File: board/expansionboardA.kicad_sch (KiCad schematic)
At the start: 66 parts, among them J1 DEBUG, J2 USB_A_Stacked, J3 HDMI_A, J4 FAN, J5 Conn_02x06_Odd_Even, J6 Conn_02x06_Odd_Even, J7 DEBUG, P1 USB_C_Plug, U1 MAX3420EECJ, U2 GPIO_U2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

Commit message: Updated board files
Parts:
- removed J5: Conn_02x06_Odd_Even, Connector_PinSocket_2.54mm:PinSocket_2x06_P2.54mm_Vertical, symbol Connector_Generic:Conn_02x06_Odd_Even
- removed J7: DEBUG, Connector_PinSocket_2.54mm:PinSocket_1x04_P2.54mm_Vertical, symbol Connector_Generic:Conn_01x04
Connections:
- net EX1 is gone; now on net LED1: U4.58 (Pin_58)
- net EX3 is gone; now on net LED2: U4.56 (Pin_56)
- net EX5 is gone; now on net LED3: U4.54 (Pin_54)
- net LED0: now also U4.60 (Pin_60); no longer U2.43 (Pin_43)
- net LED1: no longer U2.45 (Pin_45)
- net LED2: no longer U2.47 (Pin_47)
- net LED3: no longer U2.49 (Pin_49)
- net EX0: no longer names the net of U4.57 (Pin_57)
- net EX2: no longer names the net of U4.55 (Pin_55)
- net EX4: no longer names the net of U4.53 (Pin_53)
- net EX6: no longer names the net of U4.51 (Pin_51)
- net EX7: no longer names the net of U4.52 (Pin_52)
- net EX8: no longer names the net of U4.49 (Pin_49)
- net EX9: no longer names the net of U4.50 (Pin_50)
- net RXD2: no longer names the net of U4.24 (Pin_24)
- net TXD2: no longer names the net of U4.26 (Pin_26)
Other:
- note removed: "Expansion Port A"
- note removed: "UART Port B"

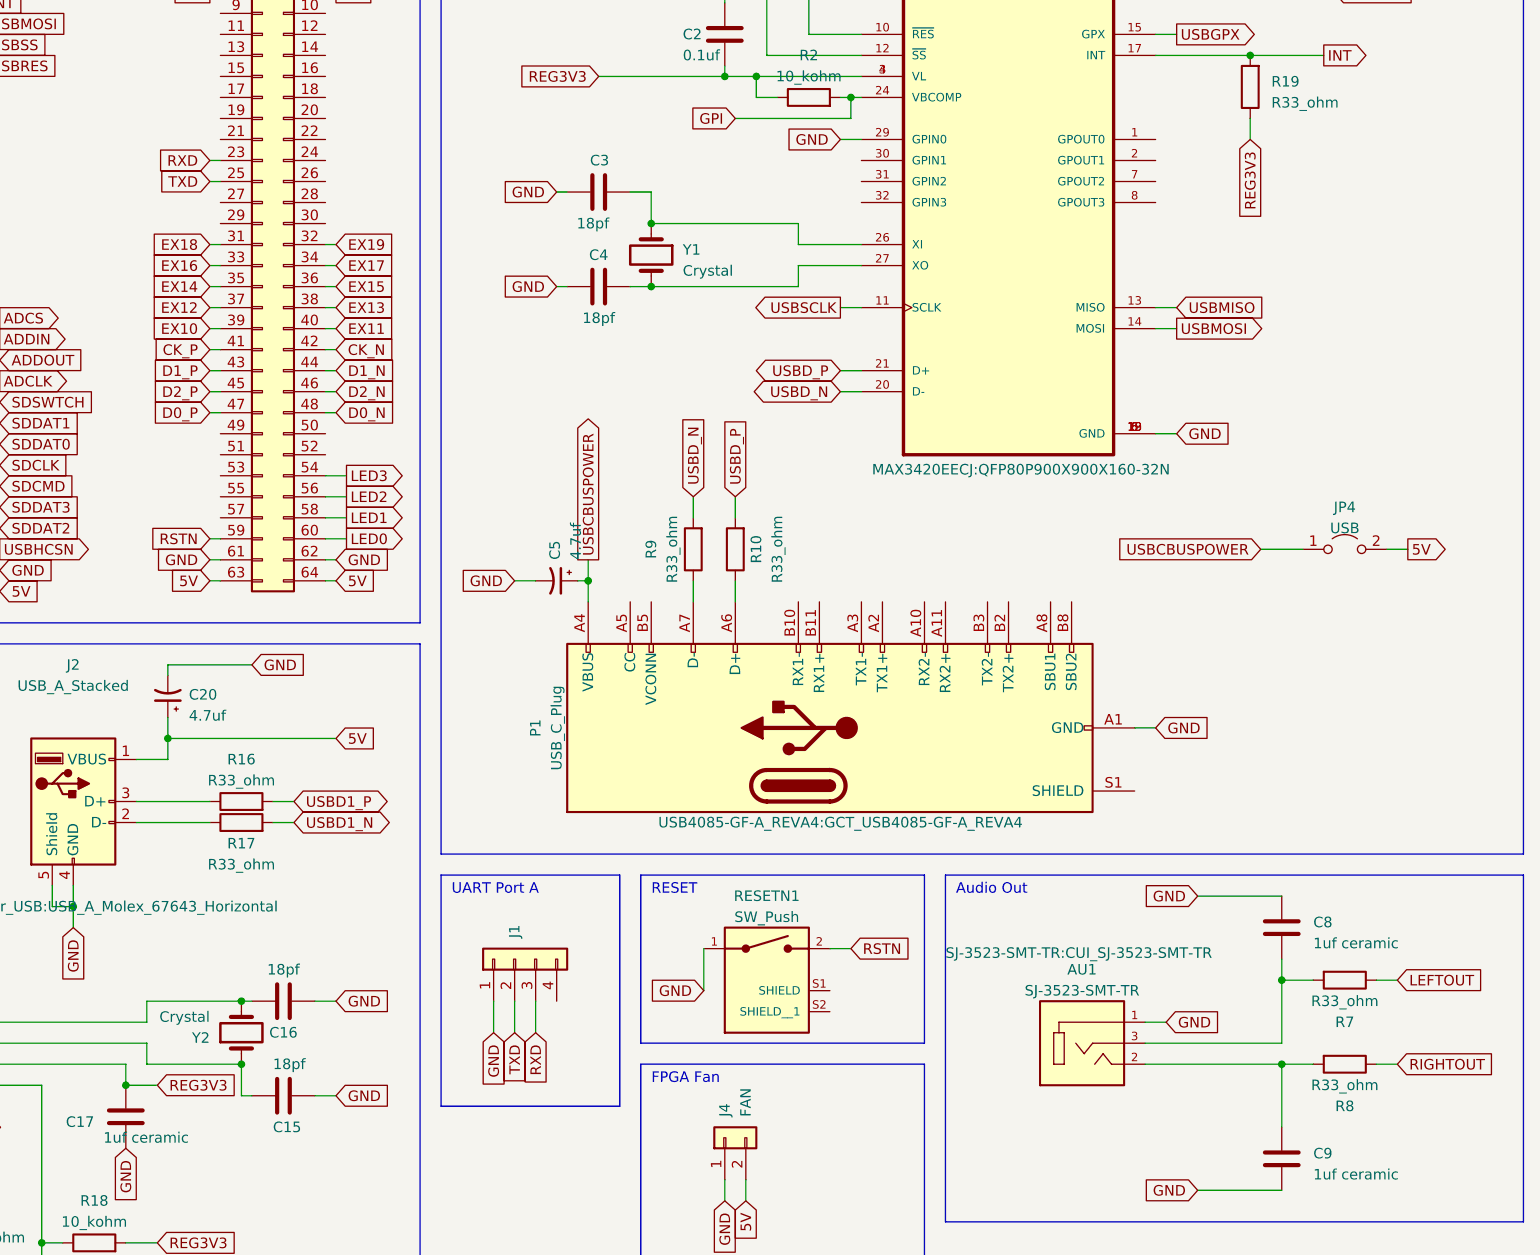
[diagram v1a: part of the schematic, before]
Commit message: Removed UART port from board and SoC
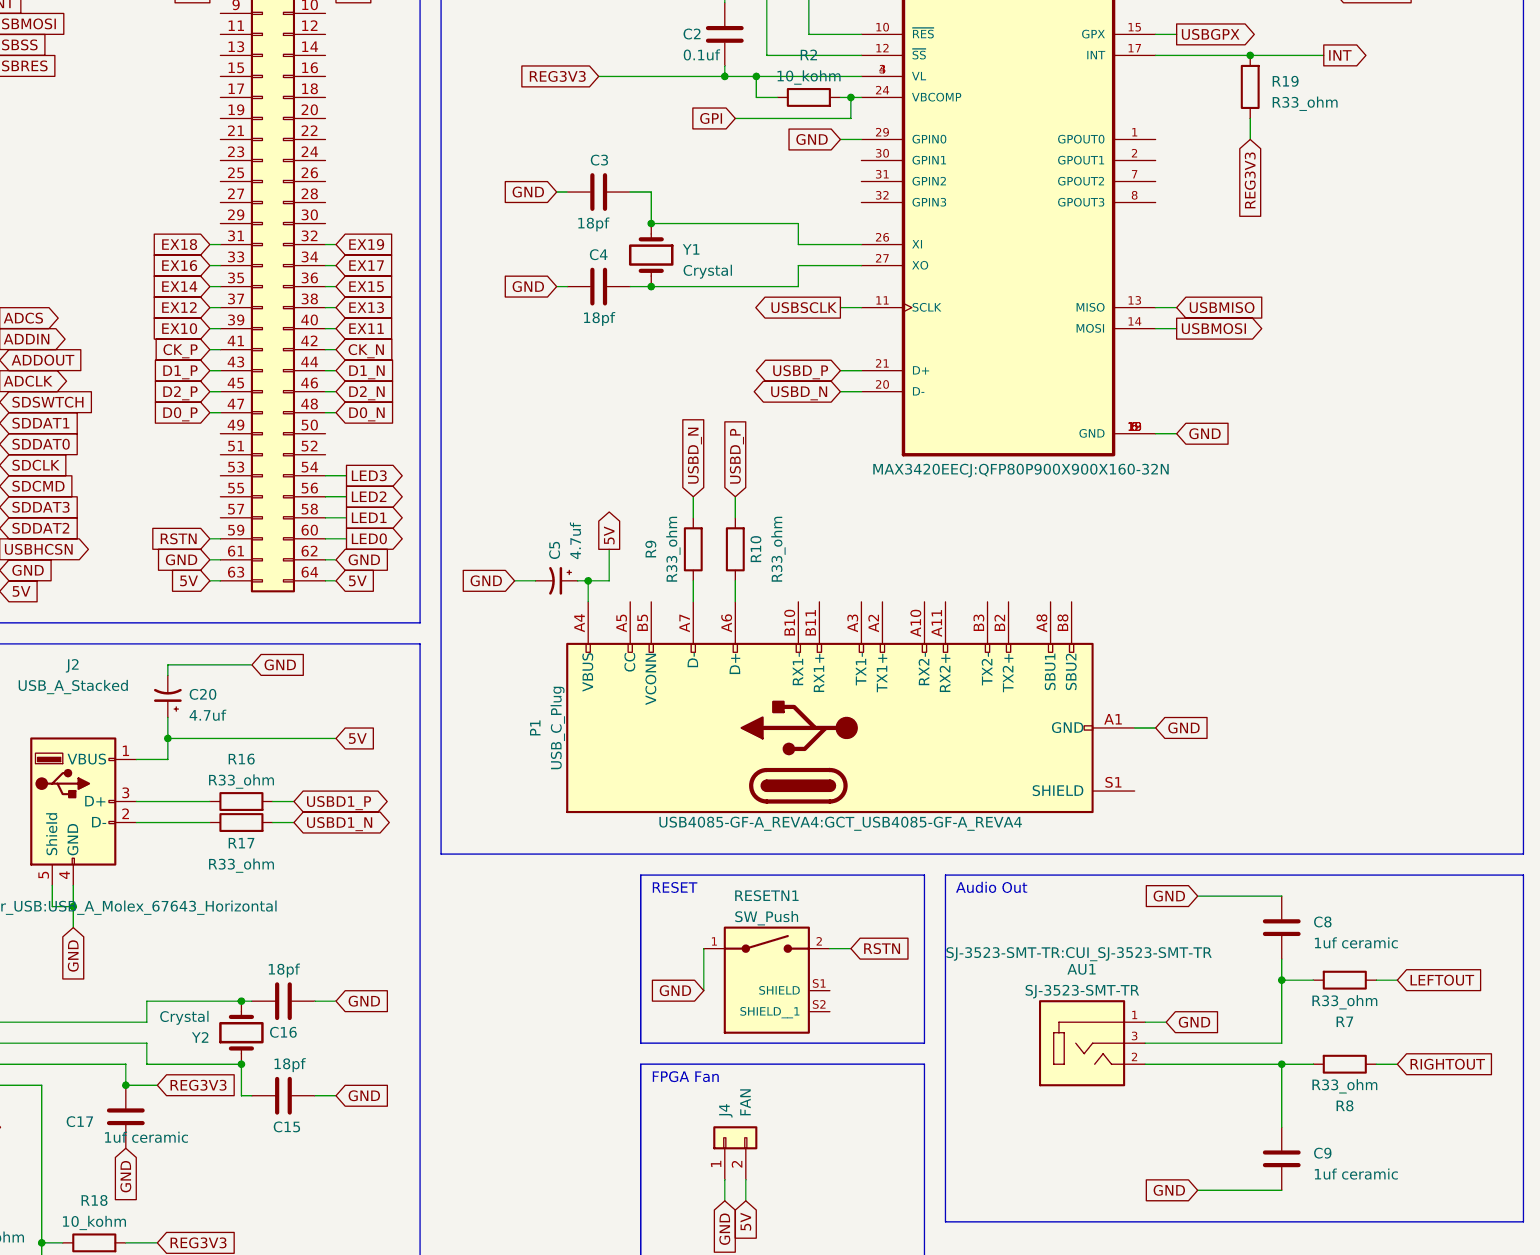
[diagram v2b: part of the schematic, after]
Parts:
- removed J1: DEBUG, Connector_PinSocket_2.54mm:PinSocket_1x04_P2.54mm_Horizontal, symbol Connector_Generic:Conn_01x04
- removed JP4: USB, Jumper:SolderJumper-2_P1.3mm_Open_Pad1.0x1.5mm, symbol Jumper:Jumper_2_Open
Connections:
- net USBCBUSPOWER is gone; now on net 5V: C5.1, P1.A4 (VBUS), P1.A9 (VBUS), P1.B4 (VBUS), P1.B9 (VBUS)
- net RXD: no longer names the net of U4.23 (Pin_23)
- net TXD: no longer names the net of U4.25 (Pin_25)
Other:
- note removed: "UART Port A"
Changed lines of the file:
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@@
     (stroke (width 0) (type default))
   )
-  (wire (pts (xy 387.35 152.4) (xy 389.89 152.4))
-    (stroke (width 0) (type default))
-  )
   (wire (pts (xy 215.9 147.32) (xy 219.71 147.32))
     (stroke (width 0) (type default))
@@
     (stroke (width 0) (type default))
   )
-  (wire (pts (xy 281.94 210.82) (xy 281.94 207.01))
-    (stroke (width 0) (type default))
-  )
   (wire (pts (xy 369.57 57.15) (xy 370.84 57.15))
     (stroke (width 0) (type default))
@@
     (stroke (width 0) (type default))
   )
-  (wire (pts (xy 284.48 210.82) (xy 284.48 207.01))
-    (stroke (width 0) (type default))
-  )
   (wire (pts (xy 219.71 129.54) (xy 215.9 129.54))
     (stroke (width 0) (type default))
   )
-  (wire (pts (xy 290.83 156.21) (xy 290.83 153.67))
+  (wire (pts (xy 293.37 156.21) (xy 293.37 152.4))
     (stroke (width 0) (type default))
   )
@@
     (stroke (width 0) (type default))
   )
-  (wire (pts (xy 372.11 152.4) (xy 377.19 152.4))
-    (stroke (width 0) (type default))
-  )
   (wire (pts (xy 359.41 173.99) (xy 356.87 173.99))
     (stroke (width 0) (type default))
@@
     (stroke (width 0) (type default))
   )
-  (wire (pts (xy 245.11 107.95) (xy 246.38 107.95))
-    (stroke (width 0) (type default))
-  )
   (wire (pts (xy 165.1 35.56) (xy 170.18 35.56))
     (stroke (width 0) (type default))
@@
     (stroke (width 0) (type default))
   )
-  (wire (pts (xy 245.11 105.41) (xy 246.38 105.41))
-    (stroke (width 0) (type default))
-  )
-  (wire (pts (xy 279.4 210.82) (xy 279.4 207.01))
-    (stroke (width 0) (type default))
-  )
   (wire (pts (xy 245.11 151.13) (xy 246.38 151.13))
     (stroke (width 0) (type default))
@@
     (stroke (width 0) (type default))
   )
+  (wire (pts (xy 293.37 156.21) (xy 290.83 156.21))
+    (stroke (width 0) (type default))
+  )
   (wire (pts (xy 378.46 49.53) (xy 381 49.53))
     (stroke (width 0) (type default))
@@
     (fill (type none))
   )
-  (rectangle (start 273.05 191.77) (end 294.64 219.71)
-    (stroke (width 0) (type default))
-    (fill (type none))
-  )
   (rectangle (start 129.54 163.83) (end 270.51 252.73)
     (stroke (width 0) (type default))
@@
     (fill (type none))
   )
-  (text "UART Port A" (at 274.32 194.31 0)
-    (effects (font (size 1.27 1.27)) (justify left bottom))
-  )
   (text "Audio Output" (at 298.45 17.78 0)
     (effects (font (size 1.27 1.27)) (justify left bottom))
@@
     )
   )
-  (global_label "USBCBUSPOWER" (shape input) (at 372.11 152.4 180) (fields_autoplaced)
-    (effects (font (size 1.27 1.27)) (justify right))
-    (property "Intersheetrefs" "${INTERSHEET_REFS}" (at 353.8433 152.4 0)
-      (effects (font (size 1.27 1.27)) (justify right) hide)
-    )
-  )
   (global_label "ADCH4" (shape input) (at 80.01 64.77 180) (fields_autoplaced)
     (effects (font (size 1.27 1.27)) (justify right))
@@
     )
   )
-  (global_label "TXD" (shape input) (at 281.94 210.82 270) (fields_autoplaced)
-    (effects (font (size 1.27 1.27)) (justify right))
-    (property "Intersheetrefs" "${INTERSHEET_REFS}" (at 281.94 217.1729 90)
-      (effects (font (size 1.27 1.27)) (justify right) hide)
-    )
-  )
   (global_label "VCC" (shape input) (at 245.11 80.01 180) (fields_autoplaced)
     (effects (font (size 1.27 1.27)) (justify right))
@@
     )
   )
-  (global_label "RXD" (shape input) (at 245.11 105.41 180) (fields_autoplaced)
-    (effects (font (size 1.27 1.27)) (justify right))
-    (property "Intersheetrefs" "${INTERSHEET_REFS}" (at 238.4547 105.41 0)
-      (effects (font (size 1.27 1.27)) (justify right) hide)
-    )
-  )
   (global_label "GND" (shape input) (at 234.95 224.79 270) (fields_autoplaced)
     (effects (font (size 1.27 1.27)) (justify right))
@@
     )
   )
-  (global_label "GND" (shape input) (at 279.4 210.82 270) (fields_autoplaced)
-    (effects (font (size 1.27 1.27)) (justify right))
-    (property "Intersheetrefs" "${INTERSHEET_REFS}" (at 279.4 217.5963 90)
-      (effects (font (size 1.27 1.27)) (justify right) hide)
-    )
-  )
   (global_label "EX11" (shape input) (at 157.48 104.14 180) (fields_autoplaced)
     (effects (font (size 1.27 1.27)) (justify right))
@@
     )
   )
-  (global_label "USBCBUSPOWER" (shape output) (at 290.83 153.67 90) (fields_autoplaced)
+  (global_label "5V" (shape output) (at 293.37 152.4 90) (fields_autoplaced)
     (effects (font (size 1.27 1.27)) (justify left))
-    (property "Intersheetrefs" "${INTERSHEET_REFS}" (at 290.83 135.4033 90)
+    (property "Intersheetrefs" "${INTERSHEET_REFS}" (at 293.37 147.1961 90)
       (effects (font (size 1.27 1.27)) (justify left) hide)
     )
@@
     )
   )
-  (global_label "TXD" (shape input) (at 245.11 107.95 180) (fields_autoplaced)
-    (effects (font (size 1.27 1.27)) (justify right))
-    (property "Intersheetrefs" "${INTERSHEET_REFS}" (at 238.7571 107.95 0)
-      (effects (font (size 1.27 1.27)) (justify right) hide)
-    )
-  )
   (global_label "AU_SCLK" (shape input) (at 311.15 29.21 180) (fields_autoplaced)
     (effects (font (size 1.27 1.27)) (justify right))
@@
     )
   )
-  (global_label "RXD" (shape input) (at 284.48 210.82 270) (fields_autoplaced)
-    (effects (font (size 1.27 1.27)) (justify right))
-    (property "Intersheetrefs" "${INTERSHEET_REFS}" (at 284.48 217.4753 90)
-      (effects (font (size 1.27 1.27)) (justify right) hide)
-    )
-  )
   (global_label "D1_P" (shape input) (at 96.52 199.39 180) (fields_autoplaced)
     (effects (font (size 1.27 1.27)) (justify right))
@@
     )
   )
-  (global_label "5V" (shape output) (at 389.89 152.4 0) (fields_autoplaced)
-    (effects (font (size 1.27 1.27)) (justify left))
-    (property "Intersheetrefs" "${INTERSHEET_REFS}" (at 395.0939 152.4 0)
-      (effects (font (size 1.27 1.27)) (justify left) hide)
-    )
-  )
   (global_label "USBGPX" (shape output) (at 361.95 90.17 0) (fields_autoplaced)
     (effects (font (size 1.27 1.27)) (justify left))
@@
     )
   )
-  (symbol (lib_id "Connector_Generic:Conn_01x04") (at 281.94 201.93 90) (unit 1)
-    (in_bom yes) (on_board yes) (dnp no)
-    (property "Reference" "J1" (at 281.9399 199.39 0)
-      (effects (font (size 1.27 1.27)) (justify left))
-    )
-    (property "Value" "DEBUG" (at 284.4799 199.39 0)
-      (effects (font (size 1.27 1.27)) (justify left) hide)
-    )
-    (property "Footprint" "Connector_PinSocket_2.54mm:PinSocket_1x04_P2.54mm_Horizontal" (at 281.94 201.93 0)
-      (effects (font (size 1.27 1.27)) hide)
-    )
-    (property "Datasheet" "~" (at 281.94 201.93 0)
-      (effects (font (size 1.27 1.27)) hide)
-    )
-    (pin "1")
-    (pin "2")
-    (pin "3")
-    (pin "4")
-    (instances
-      (project "expansionboardA"
-        (path "/317f7f3e-4535-46d0-9a87-af1bea12706a"
-          (reference "J1") (unit 1)
-        )
-      )
-    )
-  )
   (symbol (lib_id "Connector_Generic:Conn_01x02") (at 307.34 223.52 90) (unit 1)
     (in_bom yes) (on_board yes) (dnp no)
@@
         )
       )
-    )
-  )
-  (symbol (lib_id "Jumper:Jumper_2_Open") (at 382.27 152.4 0) (unit 1)
-    (in_bom yes) (on_board yes) (dnp no)
-    (property "Reference" "JP4" (at 382.27 147.32 0)
-      (effects (font (size 1.27 1.27)))
-    )
-    (property "Value" "USB" (at 382.27 149.86 0)
-      (effects (font (size 1.27 1.27)))
-    )
-    (property "Footprint" "Jumper:SolderJumper-2_P1.3mm_Open_Pad1.0x1.5mm" (at 382.27 152.4 0)
-      (effects (font (size 1.27 1.27)) hide)
-    )
-    (property "Datasheet" "~" (at 382.27 152.4 0)
-      (effects (font (size 1.27 1.27)) hide)
-    )
-    (pin "1")
-    (pin "2")
-    (instances
-      (project "expansionboardA"
-        (path "/317f7f3e-4535-46d0-9a87-af1bea12706a"
-          (reference "JP4") (unit 1)
-        )
-      )

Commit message: Board changes Rebuilt project Added qspi flash doc
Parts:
- removed J6: Conn_02x06_Odd_Even, Connector_PinSocket_2.54mm:PinSocket_2x06_P2.54mm_Vertical, symbol Connector_Generic:Conn_02x06_Odd_Even
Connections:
- net EX10: no longer names the net of U4.39 (Pin_39)
- net EX11: no longer names the net of U4.40 (Pin_40)
- net EX12: no longer names the net of U4.37 (Pin_37)
- net EX13: no longer names the net of U4.38 (Pin_38)
- net EX14: no longer names the net of U4.35 (Pin_35)
- net EX15: no longer names the net of U4.36 (Pin_36)
- net EX16: no longer names the net of U4.33 (Pin_33)
- net EX17: no longer names the net of U4.34 (Pin_34)
- net EX18: no longer names the net of U4.31 (Pin_31)
- net EX19: no longer names the net of U4.32 (Pin_32)
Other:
- note removed: "Expansion Port B"

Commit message: Logic cleanup
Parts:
- C11, C13, C14: footprint Capacitor_THT:CP_Radial_D10.0mm_P5.00mm -> Capacitor_SMD:C_0603_1608Metric_Pad1.08x0.95mm_HandSolder
- C12: footprint Capacitor_SMD:CP_Elec_6.3x5.9 -> Capacitor_SMD:C_0603_1608Metric_Pad1.08x0.95mm_HandSolder
- R11, R14: footprint Resistor_THT:R_Axial_DIN0207_L6.3mm_D2.5mm_P7.62mm_Horizontal -> Resistor_SMD:R_0603_1608Metric_Pad0.98x0.95mm_HandSolder
- R12, R13: footprint Resistor_THT:R_Axial_DIN0204_L3.6mm_D1.6mm_P5.08mm_Horizontal -> Resistor_SMD:R_0603_1608Metric_Pad0.98x0.95mm_HandSolder
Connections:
- net GND: now also U7.26 (GPIN0)
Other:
- note added: "USB Host"
- note added: "USB Power / Data"
- note removed: "USB HOST"
- note removed: "USB-C Power and Data"
- moved on the sheet: ADC1, CRD1, LSRIGHT1, U5

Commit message: SDK/sample/board fixes Updated ROM image
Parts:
- ADC1: footprint Connector_PinSocket_2.54mm:PinSocket_2x05_P2.54mm_Horizontal -> Connector_PinSocket_2.54mm:PinSocket_2x05_P2.54mm_Vertical
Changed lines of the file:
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@@
       (effects (font (size 1.27 1.27)) (justify left))
     )
-    (property "Footprint" "Connector_PinSocket_2.54mm:PinSocket_2x05_P2.54mm_Horizontal" (at 147.32 101.6 0)
+    (property "Footprint" "Connector_PinSocket_2.54mm:PinSocket_2x05_P2.54mm_Vertical" (at 147.32 101.6 0)
       (effects (font (size 1.27 1.27)) hide)
     )

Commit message: Updated board files
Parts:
- ADC1: footprint Connector_PinSocket_2.54mm:PinSocket_2x05_P2.54mm_Vertical -> Connector_PinSocket_2.54mm:PinSocket_2x05_P2.54mm_Horizontal
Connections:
- net LED0: now also U4.53 (Pin_53); no longer U4.60 (Pin_60)
- net LED1: now also U4.55 (Pin_55); no longer U4.58 (Pin_58)
- net LED2: now also U4.57 (Pin_57); no longer U4.56 (Pin_56)
- net LED3: now also U4.59 (Pin_59); no longer U4.54 (Pin_54)
- net RSTN: now also U4.60 (Pin_60); no longer U4.59 (Pin_59)
